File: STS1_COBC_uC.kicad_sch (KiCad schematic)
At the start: 43 parts, among them IC2 STWD100PYW83F, IC3 STM32F411RET6TR, J12 Conn_01x01_Male, J13 Conn_01x01_Male, J16 Conn_ARM_JTAG_SWD_10, J17 Conn_01x03_Male, J3 Conn_01x01_Male, J4 Conn_01x01_Male, J6 Conn_01x01_Male, J7 Conn_01x01_Male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

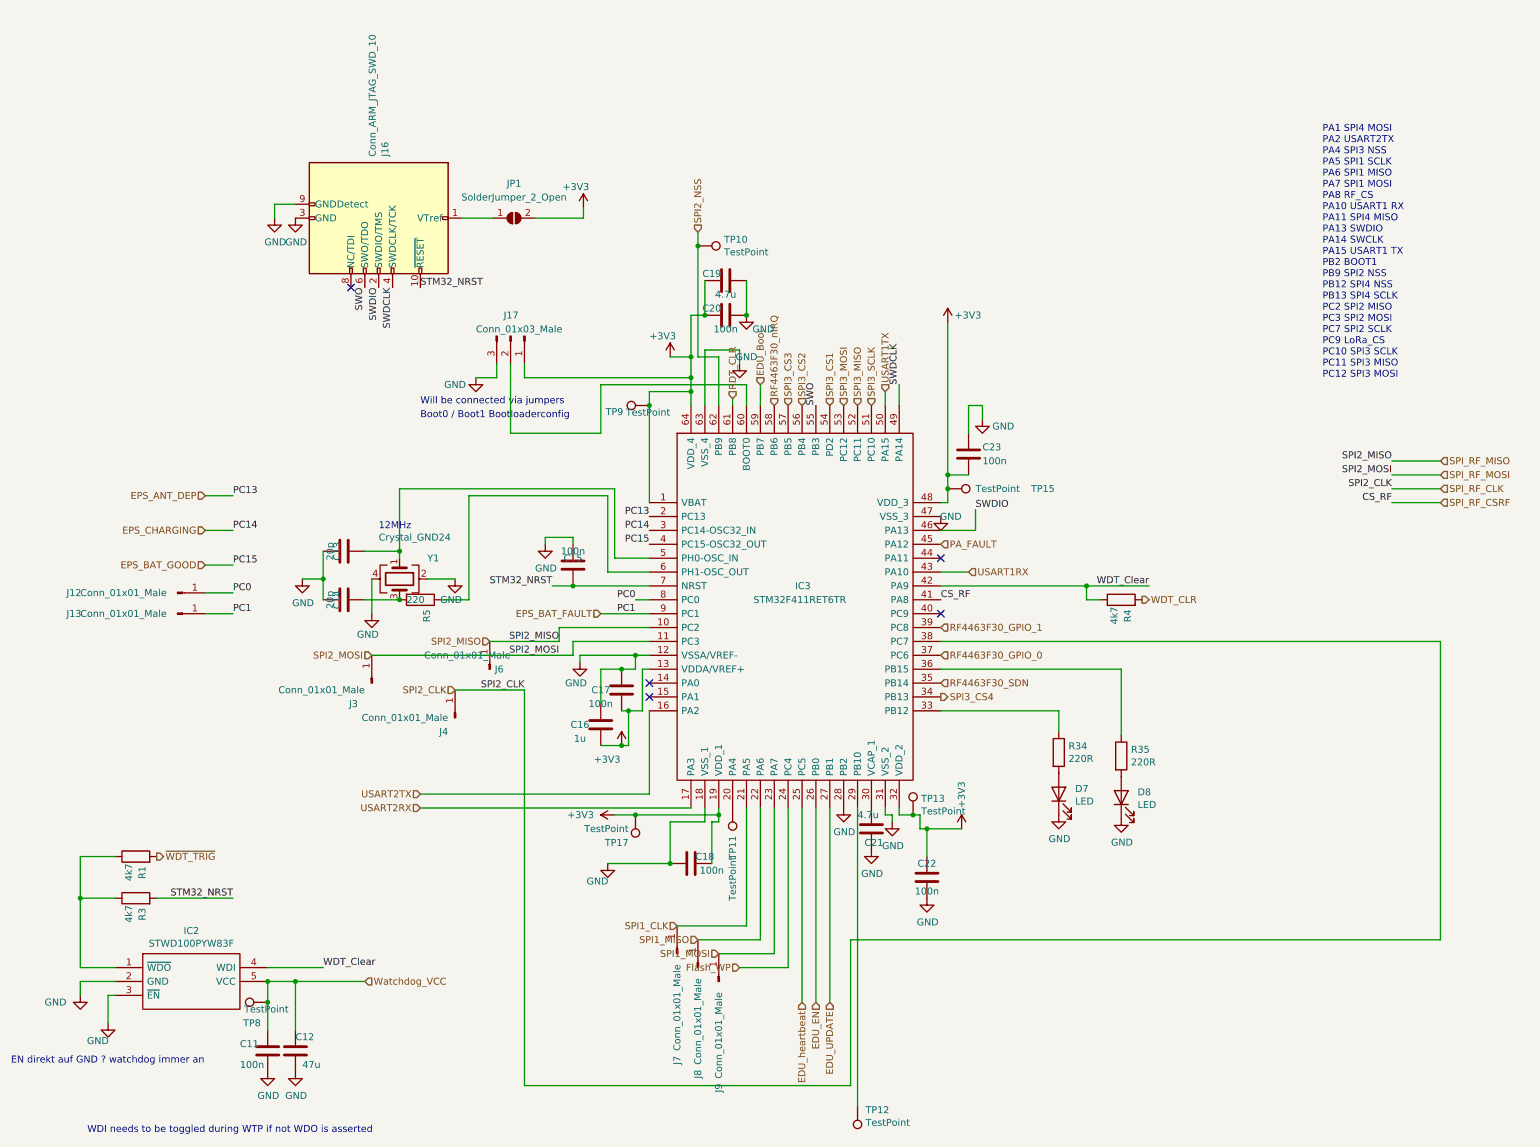
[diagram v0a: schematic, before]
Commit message: feat: clean up schematic
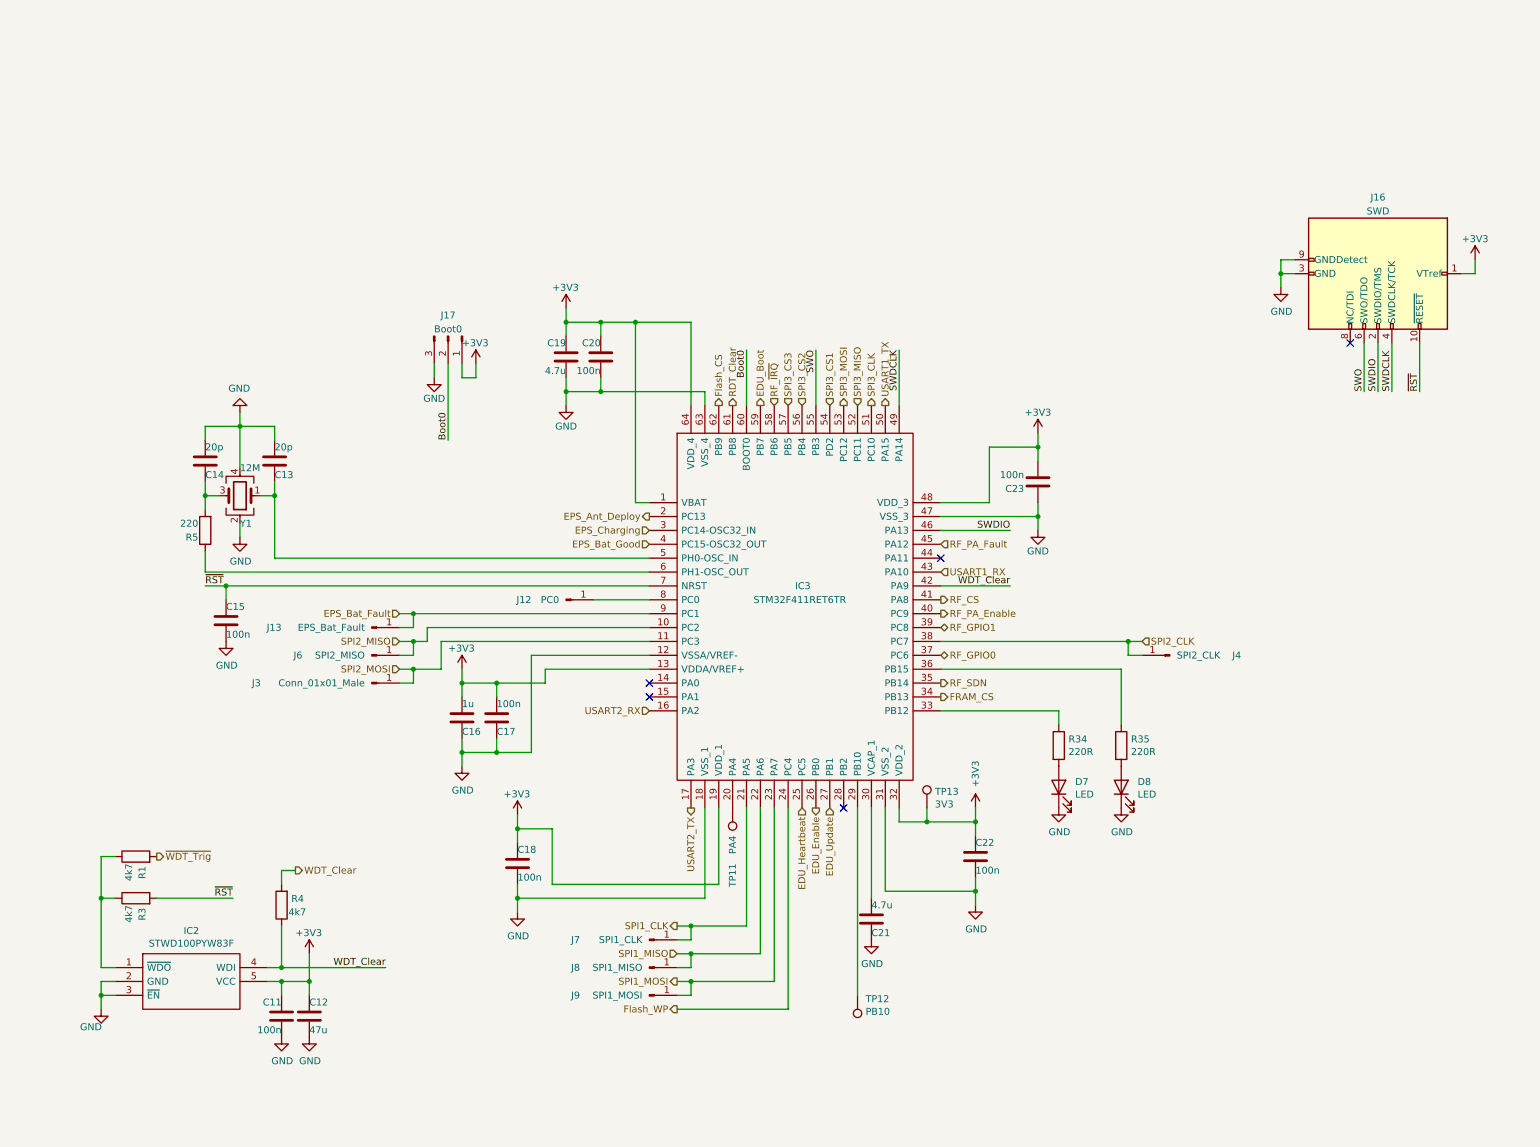
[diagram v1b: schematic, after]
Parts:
- removed JP1: SolderJumper_2_Open, Jumper:SolderJumper-2_P1.3mm_Open_TrianglePad1.0x1.5mm, symbol Jumper:SolderJumper_2_Open
- removed TP10, TP15, TP17, TP8, TP9: TestPoint, STS1library:STS1_Testpoint, symbol Connector:TestPoint
- J12: value Conn_01x01_Male -> PC0
- J13: value Conn_01x01_Male -> EPS_Bat_Fault
- J16: value Conn_ARM_JTAG_SWD_10 -> SWD
- J17: value Conn_01x03_Male -> Boot0
- J4: value Conn_01x01_Male -> SPI2_CLK
- J6: value Conn_01x01_Male -> SPI2_MISO
- J7: value Conn_01x01_Male -> SPI1_CLK
- J8: value Conn_01x01_Male -> SPI1_MISO
- J9: value Conn_01x01_Male -> SPI1_MOSI
- TP11: value TestPoint -> PA4
- TP12: value TestPoint -> PB10
- TP13: value TestPoint -> 3V3
- Y1: value Crystal_GND24 -> 12M
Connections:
- net WDT_CLR is gone; now on net WDT_Clear: R4.2
- net Watchdog_VCC is gone; now on net +3V3: C11.1, C12.1, IC2.5 (VCC)
- net +3V3: now also J16.1 (VTref)
- net GND: no longer IC3.28 (PB2)
- net RF_PA_Enable: now reaches IC3.40 (PC9)
- net Boot0: now reaches IC3.60 (BOOT0), J17.2 (Pin_2)
- net EDU_EN renamed EDU_Enable
- net EDU_UPDATE renamed EDU_Update
- net EDU_heartbeat renamed EDU_Heartbeat
- net EPS_ANT_DEP renamed EPS_Ant_Deploy
- net EPS_BAT_FAULT renamed EPS_Bat_Fault
- net EPS_BAT_GOOD renamed EPS_Bat_Good
- net EPS_CHARGING renamed EPS_Charging
- net PA_FAULT renamed RF_PA_Fault
- net PC0: no longer names the net of IC3.8 (PC0), J12.1 (Pin_1)
- net RDT_CLR renamed RDT_Clear
- net RF4463F30_GPIO_0 renamed RF_GPIO0
- net RF4463F30_GPIO_1 renamed RF_GPIO1
- net RF4463F30_SDN renamed RF_SDN
- net RF4463F30_nIRQ renamed RF_~{IRQ}
- net SPI2_NSS renamed Flash_CS
- net SPI3_CS4 renamed FRAM_CS
- net SPI3_SCLK renamed SPI3_CLK
- net SPI_RF_CSRF renamed RF_CS
- net STM32_NRST renamed ~{RST}
- net USART1RX renamed USART1_RX
- net USART1TX renamed USART1_TX
- net USART2RX renamed USART2_TX
- net USART2TX renamed USART2_RX
- net ~{WDT_TRIG} renamed ~{WDT_Trig}
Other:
- note removed: "12MHz"
- note removed: "Boot0 / Boot1 Bootloaderconfig"
- note removed: "EN direkt auf GND ? watchdog immer an"
- note removed: "PA1 SPI4 MOSI PA2 USART2TX PA4 SPI3 NSS PA5 SPI1 SCLK PA6 SPI1 MISO PA7 SPI1 MOSI PA8 RF_CS PA10 USART1 RX PA11 SPI4 MISO PA13 SWDIO PA14 SWCLK PA15 USART1 TX PB2 BOOT1 PB9 SPI2 NSS PB12 SPI4 NSS PB13 SPI4 SCLK PC2 SPI2 MISO PC3 SPI2 MOSI PC7 SPI2 SCLK PC9 LoRa_CS PC10 SPI3 SCLK PC11 SPI3 MISO PC12 SPI3 MOSI"
- note removed: "WDI needs to be toggled during WTP if not WDO is asserted"
- note removed: "Will be connected via jumpers"
- moved on the sheet: C11, C12, C13, C14, C15, C16, C17, C18, C19, C20, C21, C22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

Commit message: feat: update RF hardware and clean up ERC errors
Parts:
- IC2: footprint SamacSys_Parts:SOT65P210X110-5N -> SOT65P210X110-5N
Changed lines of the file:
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@@
     (pin "2")
   )
-  (symbol (lib_name "GND_8") (lib_id "power:GND") (at 46.99 83.82 0) (unit 1)
+  (symbol (lib_id "power:GND") (at 46.99 83.82 0) (unit 1)
     (in_bom yes) (on_board yes)
     (property "Reference" "#PWR051" (id 0) (at 46.99 90.17 0)
@@
     (pin "1")
   )
-  (symbol (lib_name "GND_17") (lib_id "power:GND") (at 181.61 151.13 0) (unit 1)
+  (symbol (lib_id "power:GND") (at 181.61 151.13 0) (unit 1)
     (in_bom yes) (on_board yes)
     (property "Reference" "#PWR068" (id 0) (at 181.61 157.48 0)
@@
     (pin "1")
   )
-  (symbol (lib_name "GND_14") (lib_id "power:GND") (at 162.56 157.48 0) (unit 1)
+  (symbol (lib_id "power:GND") (at 162.56 157.48 0) (unit 1)
     (in_bom yes) (on_board yes)
     (property "Reference" "#PWR066" (id 0) (at 162.56 163.83 0)
@@
     (pin "1")
   )
-  (symbol (lib_name "GND_4") (lib_id "power:GND") (at 82.55 54.61 0) (unit 1)
+  (symbol (lib_id "power:GND") (at 82.55 54.61 0) (unit 1)
     (in_bom yes) (on_board yes)
     (property "Reference" "#PWR056" (id 0) (at 82.55 60.96 0)
@@
     (property "Reference" "IC2" (id 0) (at 38.1 155.829 0))
     (property "Value" "STWD100PYW83F" (id 1) (at 38.1 158.1404 0))
-    (property "Footprint" "SamacSys_Parts:SOT65P210X110-5N" (id 2) (at 48.26 160.02 0)
+    (property "Footprint" "SOT65P210X110-5N" (id 2) (at 48.26 160.02 0)
       (effects (font (size 1.27 1.27)) (justify left) hide)
     )
@@
     (pin "5")
   )
-  (symbol (lib_name "GND_3") (lib_id "power:GND") (at 21.59 170.18 0) (unit 1)
+  (symbol (lib_id "power:GND") (at 21.59 170.18 0) (unit 1)
     (in_bom yes) (on_board yes)
     (property "Reference" "#PWR045" (id 0) (at 21.59 176.53 0)
@@
     (pin "2")
   )
-  (symbol (lib_name "GND_2") (lib_id "power:GND") (at 59.69 175.26 0) (unit 1)
+  (symbol (lib_id "power:GND") (at 59.69 175.26 0) (unit 1)
     (in_bom yes) (on_board yes)
     (property "Reference" "#PWR050" (id 0) (at 59.69 181.61 0)
@@
     (pin "1")
   )
-  (symbol (lib_name "GND_1") (lib_id "power:GND") (at 54.61 175.26 0) (unit 1)
+  (symbol (lib_id "power:GND") (at 54.61 175.26 0) (unit 1)
     (in_bom yes) (on_board yes)
     (property "Reference" "#PWR047" (id 0) (at 54.61 181.61 0)
@@
     (pin "2")
   )
-  (symbol (lib_name "GND_13") (lib_id "power:GND") (at 44.45 102.87 0) (unit 1)
+  (symbol (lib_id "power:GND") (at 44.45 102.87 0) (unit 1)
     (in_bom yes) (on_board yes)
     (property "Reference" "#PWR057" (id 0) (at 44.45 109.22 0)
@@
     (pin "1")
   )
-  (symbol (lib_name "+3V3_1") (lib_id "power:+3V3") (at 90.17 52.07 0) (unit 1)
+  (symbol (lib_id "power:+3V3") (at 90.17 52.07 0) (unit 1)
     (in_bom yes) (on_board yes)
     (property "Reference" "#PWR062" (id 0) (at 90.17 55.88 0)
@@
     (pin "1")
   )
-  (symbol (lib_name "+3V3_5") (lib_id "power:+3V3") (at 181.61 133.35 0) (unit 1)
+  (symbol (lib_id "power:+3V3") (at 181.61 133.35 0) (unit 1)
     (in_bom yes) (on_board yes)
     (property "Reference" "#PWR072" (id 0) (at 181.61 137.16 0)
@@
     (pin "9")
   )
-  (symbol (lib_name "GND_5") (lib_id "power:GND") (at 237.49 38.1 0) (unit 1)
+  (symbol (lib_id "power:GND") (at 237.49 38.1 0) (unit 1)
     (in_bom yes) (on_board yes)
     (property "Reference" "#PWR049" (id 0) (at 237.49 44.45 0)
@@
     (pin "1")
   )
-  (symbol (lib_name "+3V3_2") (lib_id "power:+3V3") (at 273.05 33.02 0) (unit 1)
+  (symbol (lib_id "power:+3V3") (at 273.05 33.02 0) (unit 1)
     (in_bom yes) (on_board yes)
     (property "Reference" "#PWR055" (id 0) (at 273.05 36.83 0)
@@
     (pin "1")
   )
-  (symbol (lib_name "GND_16") (lib_id "power:GND") (at 196.85 133.35 0) (unit 1)
+  (symbol (lib_id "power:GND") (at 196.85 133.35 0) (unit 1)
     (in_bom yes) (on_board yes)
     (property "Reference" "#PWR0107" (id 0) (at 196.85 139.7 0)
@@
     (pin "1")
   )
-  (symbol (lib_name "+3V3_1") (lib_id "power:+3V3") (at 97.79 134.62 0) (unit 1)
+  (symbol (lib_id "power:+3V3") (at 97.79 134.62 0) (unit 1)
     (in_bom yes) (on_board yes)
     (property "Reference" "#PWR0112" (id 0) (at 97.79 138.43 0)
@@
     (pin "1")
   )
-  (symbol (lib_name "GND_4") (lib_id "power:GND") (at 106.68 59.69 0) (unit 1)
+  (symbol (lib_id "power:GND") (at 106.68 59.69 0) (unit 1)
     (in_bom yes) (on_board yes)
     (property "Reference" "#PWR0115" (id 0) (at 106.68 66.04 0)
@@
     (pin "2")
   )
-  (symbol (lib_name "+3V3_1") (lib_id "power:+3V3") (at 87.63 107.95 0) (unit 1)
+  (symbol (lib_id "power:+3V3") (at 87.63 107.95 0) (unit 1)
     (in_bom yes) (on_board yes)
     (property "Reference" "#PWR0111" (id 0) (at 87.63 111.76 0)
@@
     (pin "1")
   )
-  (symbol (lib_name "GND_15") (lib_id "power:GND") (at 208.28 133.35 0) (unit 1)
+  (symbol (lib_id "power:GND") (at 208.28 133.35 0) (unit 1)
     (in_bom yes) (on_board yes)
     (property "Reference" "#PWR0108" (id 0) (at 208.28 139.7 0)
@@
     (pin "1")
   )
-  (symbol (lib_name "+3V3_1") (lib_id "power:+3V3") (at 59.69 160.02 0) (unit 1)
+  (symbol (lib_id "power:+3V3") (at 59.69 160.02 0) (unit 1)
     (in_bom yes) (on_board yes)
     (property "Reference" "#PWR0110" (id 0) (at 59.69 163.83 0)
@@
     (pin "1")
   )
-  (symbol (lib_name "GND_13") (lib_id "power:GND") (at 87.63 125.73 0) (unit 1)
+  (symbol (lib_id "power:GND") (at 87.63 125.73 0) (unit 1)
     (in_bom yes) (on_board yes)
     (property "Reference" "#PWR0113" (id 0) (at 87.63 132.08 0)
@@
     (pin "2")
   )
-  (symbol (lib_name "+3V3_1") (lib_id "power:+3V3") (at 106.68 41.91 0) (unit 1)
+  (symbol (lib_id "power:+3V3") (at 106.68 41.91 0) (unit 1)
     (in_bom yes) (on_board yes)
     (property "Reference" "#PWR0117" (id 0) (at 106.68 45.72 0)
@@
     (pin "1")
   )
-  (symbol (lib_name "GND_8") (lib_id "power:GND") (at 46.99 60.96 180) (unit 1)
+  (symbol (lib_id "power:GND") (at 46.99 60.96 180) (unit 1)
     (in_bom yes) (on_board yes)
     (property "Reference" "#PWR0114" (id 0) (at 46.99 54.61 0)
@@
     (pin "2")
   )
-  (symbol (lib_name "GND_13") (lib_id "power:GND") (at 97.79 152.4 0) (unit 1)
+  (symbol (lib_id "power:GND") (at 97.79 152.4 0) (unit 1)
     (in_bom yes) (on_board yes)
     (property "Reference" "#PWR0116" (id 0) (at 97.79 158.75 0)

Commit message: feat: more schematic cleanup
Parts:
- C12: value 47u -> 47µ
- C16: value 1u -> 1µ
- C19, C21: value 4.7u -> 4.7µ
- IC2: footprint SOT65P210X110-5N -> SamacSys_Parts:SOT65P210X110-5N
- R1, R3, R4: value 4k7 -> 4.7k
- R34, R35: value 220R -> 220
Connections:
- net Flash_WP renamed Flash_~{WP}
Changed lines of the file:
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@@
-    (stroke (width 0) (type default) (color 0 0 0 0))
-  )
-  (wire (pts (xy 147.32 170.18) (xy 147.32 133.35))
     (stroke (width 0) (type default) (color 0 0 0 0))
   )
@@
   )
   (wire (pts (xy 90.17 52.07) (xy 90.17 54.61))
-    (stroke (width 0) (type default) (color 0 0 0 0))
-  )
-  (wire (pts (xy 127 170.18) (xy 147.32 170.18))
     (stroke (width 0) (type default) (color 0 0 0 0))
   )
@@
     (effects (font (size 1.27 1.27)) (justify left))
   )
-  (hierarchical_label "Flash_WP" (shape output) (at 127 170.18 180)
+  (hierarchical_label "Flash_~{WP}" (shape output) (at 147.32 133.35 270)
     (effects (font (size 1.27 1.27)) (justify right))
   )
@@
       (effects (font (size 1.27 1.27)) (justify left))
     )
-    (property "Value" "4.7u" (id 1) (at 162.56 151.13 0)
+    (property "Value" "4.7µ" (id 1) (at 162.56 151.13 0)
       (effects (font (size 1.27 1.27)) (justify left))
     )
@@
       (effects (font (size 1.27 1.27)) (justify left))
     )
-    (property "Value" "4.7u" (id 1) (at 106.68 53.34 0)
+    (property "Value" "4.7µ" (id 1) (at 106.68 53.34 0)
       (effects (font (size 1.27 1.27)) (justify left))
     )
@@
       (effects (font (size 1.27 1.27)) (justify left))
     )
-    (property "Value" "1u" (id 1) (at 87.63 114.3 0)
+    (property "Value" "1µ" (id 1) (at 87.63 114.3 0)
       (effects (font (size 1.27 1.27)) (justify left))
     )
@@
       (effects (font (size 1.27 1.27)) (justify right))
     )
-    (property "Value" "4k7" (id 1) (at 26.67 151.13 0)
+    (property "Value" "4.7k" (id 1) (at 26.67 151.13 0)
       (effects (font (size 1.27 1.27)) (justify right))
     )
@@
     (property "Reference" "IC2" (id 0) (at 38.1 155.829 0))
     (property "Value" "STWD100PYW83F" (id 1) (at 38.1 158.1404 0))
-    (property "Footprint" "SOT65P210X110-5N" (id 2) (at 48.26 160.02 0)
+    (property "Footprint" "SamacSys_Parts:SOT65P210X110-5N" (id 2) (at 48.26 160.02 0)
       (effects (font (size 1.27 1.27)) (justify left) hide)
     )
@@
       (effects (font (size 1.27 1.27)) (justify left))
     )
-    (property "Value" "47u" (id 1) (at 59.69 173.99 0)
+    (property "Value" "47µ" (id 1) (at 59.69 173.99 0)
       (effects (font (size 1.27 1.27)) (justify left))
     )
@@
       (effects (font (size 1.27 1.27)) (justify left))
     )
-    (property "Value" "220R" (id 1) (at 210.058 123.063 0)
+    (property "Value" "220" (id 1) (at 210.058 123.063 0)
       (effects (font (size 1.27 1.27)) (justify left))
     )
@@
       (effects (font (size 1.27 1.27)) (justify right))
     )
-    (property "Value" "4k7" (id 1) (at 26.67 143.51 0)
+    (property "Value" "4.7k" (id 1) (at 26.67 143.51 0)
       (effects (font (size 1.27 1.27)) (justify right))
     )
@@
       (effects (font (size 1.27 1.27)) (justify left))
     )
-    (property "Value" "220R" (id 1) (at 198.628 123.063 0)
+    (property "Value" "220" (id 1) (at 198.628 123.063 0)
       (effects (font (size 1.27 1.27)) (justify left))
     )
@@
       (effects (font (size 1.27 1.27)) (justify right))
     )
-    (property "Value" "4k7" (id 1) (at 55.88 152.4 0)
-      (effects (font (size 1.27 1.27)) (justify right))
-    )
+    (property "Value" "4.7k" (id 1) (at 55.88 152.4 0)
+      (effects (font (size 1.27 1.27)) (justify right))
+    )

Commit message: feat: layout changed for new RF part
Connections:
- net WDT_Clear: no longer IC2.4 (WDI), IC3.42 (PA9), R4.1
- new net WDT_Clear_In: IC2.4 (WDI), IC3.42 (PA9), R4.1
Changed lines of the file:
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@@
     (effects (font (size 1.27 1.27)) (justify left bottom))
   )
-  (label "WDT_Clear" (at 73.66 162.56 180)
+  (label "WDT_Clear_In" (at 73.66 162.56 180)
     (effects (font (size 1.27 1.27)) (justify right bottom))
   )
@@
     (effects (font (size 1.27 1.27)) (justify left bottom))
   )
-  (label "WDT_Clear" (at 187.96 92.71 180)
+  (label "WDT_Clear_In" (at 187.96 92.71 180)
     (effects (font (size 1.27 1.27)) (justify right bottom))
   )

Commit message: Fix footprint assignments: all IC should have U designator
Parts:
- renumbered IC2 to U18, IC3 to U19
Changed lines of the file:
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@@
   (symbol (lib_id "STS1_COBC_V2-rescue:STM32F411RET6TR-STM32F411RET6TR") (at 121.92 77.47 0) (unit 1)
     (in_bom yes) (on_board yes)
-    (property "Reference" "IC3" (id 0) (at 148.59 92.71 0)
+    (property "Reference" "U19" (id 0) (at 148.59 92.71 0)
       (effects (font (size 1.27 1.27)) (justify left))
     )
@@
   (symbol (lib_id "SamacSys_Parts:STWD100PYW83F") (at 24.13 162.56 0) (unit 1)
     (in_bom yes) (on_board yes)
-    (property "Reference" "IC2" (id 0) (at 38.1 155.829 0))
+    (property "Reference" "U18" (id 0) (at 38.1 155.829 0))
     (property "Value" "STWD100PYW83F" (id 1) (at 38.1 158.1404 0))
     (property "Footprint" "SamacSys_Parts:SOT65P210X110-5N" (id 2) (at 48.26 160.02 0)

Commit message: Fix footprint assignments: all CSBI headers should have J designator
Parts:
- renumbered U18 to IC2, U19 to IC3
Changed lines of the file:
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@@
   (symbol (lib_id "STS1_COBC_V2-rescue:STM32F411RET6TR-STM32F411RET6TR") (at 121.92 77.47 0) (unit 1)
     (in_bom yes) (on_board yes)
-    (property "Reference" "U19" (id 0) (at 148.59 92.71 0)
+    (property "Reference" "IC3" (id 0) (at 148.59 92.71 0)
       (effects (font (size 1.27 1.27)) (justify left))
     )
@@
   (symbol (lib_id "SamacSys_Parts:STWD100PYW83F") (at 24.13 162.56 0) (unit 1)
     (in_bom yes) (on_board yes)
-    (property "Reference" "U18" (id 0) (at 38.1 155.829 0))
+    (property "Reference" "IC2" (id 0) (at 38.1 155.829 0))
     (property "Value" "STWD100PYW83F" (id 1) (at 38.1 158.1404 0))
     (property "Footprint" "SamacSys_Parts:SOT65P210X110-5N" (id 2) (at 48.26 160.02 0)

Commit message: Exclude jumpers, mounting holes, fiducials etc. from BOM
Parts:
- TP11, TP12: now left out of the parts list
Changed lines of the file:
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@@
   )
   (symbol (lib_id "Connector:TestPoint") (at 160.02 167.64 180) (unit 1)
-    (in_bom yes) (on_board yes)
+    (in_bom no) (on_board yes)
     (property "Reference" "TP12" (id 0) (at 161.4932 168.3004 0)
       (effects (font (size 1.27 1.27)) (justify right))
@@
   )
   (symbol (lib_id "Connector:TestPoint") (at 137.16 133.35 180) (unit 1)
-    (in_bom yes) (on_board yes)
+    (in_bom no) (on_board yes)
     (property "Reference" "TP11" (id 0) (at 137.16 143.51 90)
       (effects (font (size 1.27 1.27)) (justify left))
